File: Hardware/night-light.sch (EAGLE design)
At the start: 52 parts, among them Q1 8/16/20MHz, U1 ATMEGA328, U2 MIC5205

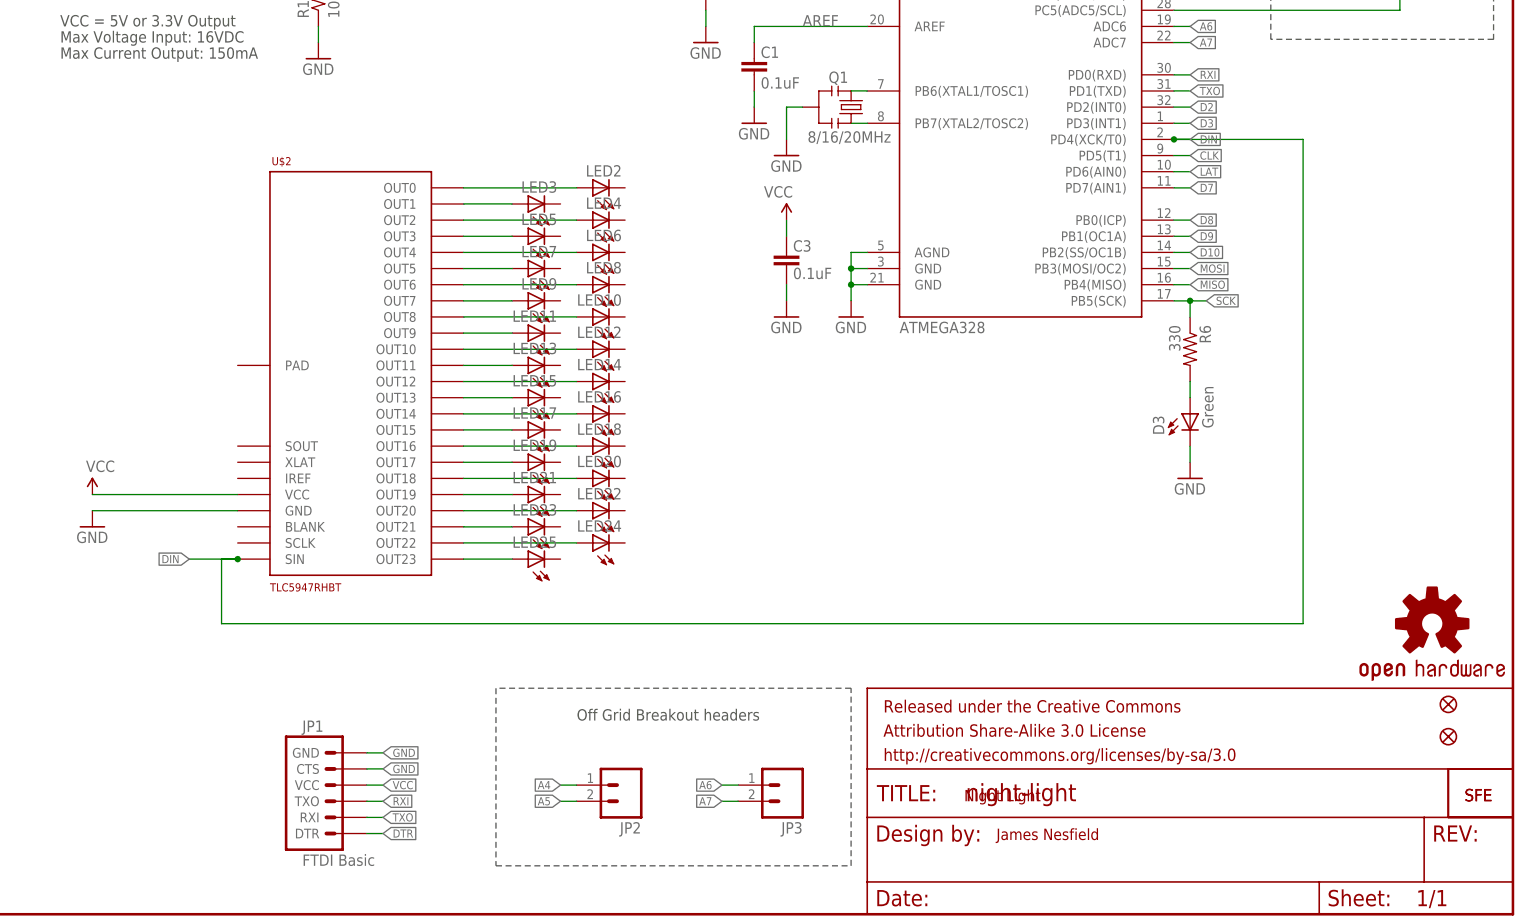
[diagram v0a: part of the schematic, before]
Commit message: added tlc5947
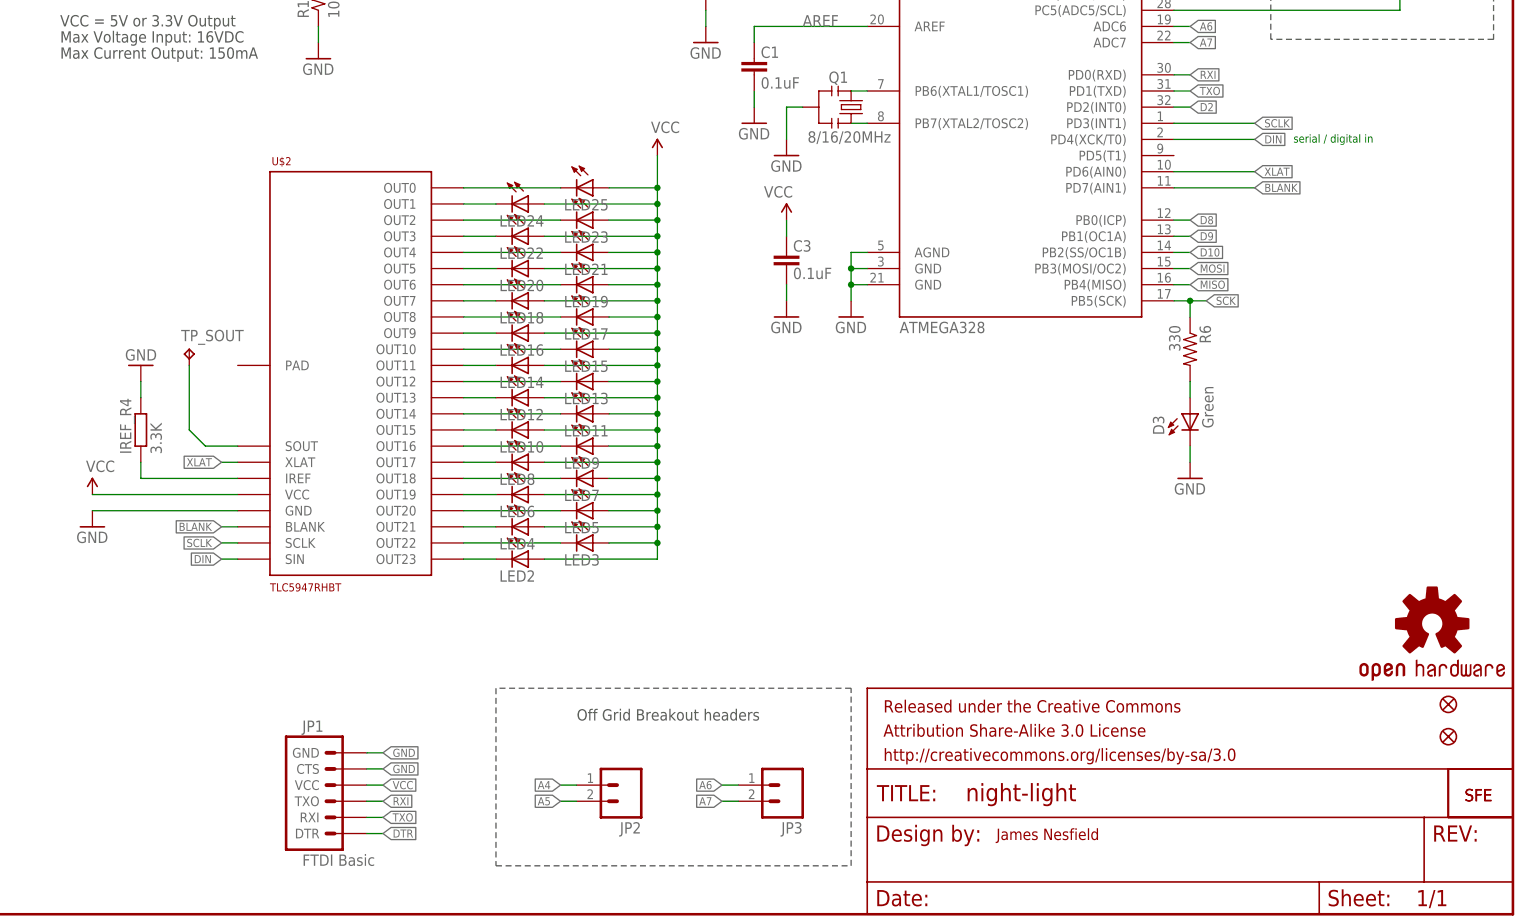
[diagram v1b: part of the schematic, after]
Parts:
- added IREF_R4: 3.3K, eagle-ltspice:RR0603
- added TP_SOUT: TPTP20R, testpad:TPTP20R
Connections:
- removed net CLK: U1.PD5(T1)
- removed net D3: U1.PD3(INT1)
- removed net D7: U1.PD7(AIN1)
- removed net LAT: U1.PD6(AIN0)
- new net BLANK: U$2.BLANK, U1.PD7(AIN1)
- new net N$30: LED3.C, U$2.OUT22
- new net N$31: LED2.C, U$2.OUT23
- new net SCLK: U$2.SCLK, U1.PD3(INT1)
- new net XLAT: U$2.XLAT, U1.PD6(AIN0)
- net 3.3V: now also LED10.A, LED11.A, LED12.A, LED13.A, LED14.A, LED15.A, LED16.A, LED17.A, LED18.A, LED19.A, LED2.A, LED20.A, LED21.A, LED22.A, LED23.A, LED24.A, LED25.A, LED3.A, LED4.A, LED5.A, LED6.A, LED7.A, LED8.A, LED9.A
- net GND: now also IREF_R4.2
- net N$10: now also LED23.C, U$2.OUT2; no longer LED6.A, U$2.OUT4
- net N$11: now also LED22.C, U$2.OUT3; no longer LED7.A, U$2.OUT5
- net N$12: now also LED21.C, U$2.OUT4; no longer LED8.A, U$2.OUT6
- net N$13: now also LED20.C, U$2.OUT5; no longer LED9.A, U$2.OUT7
- net N$14: now also LED19.C, U$2.OUT6; no longer LED10.A, U$2.OUT8
- net N$15: now also LED18.C, U$2.OUT7; no longer LED11.A, U$2.OUT9
- net N$16: now also LED17.C, U$2.OUT8; no longer LED12.A, U$2.OUT10
- net N$17: now also LED16.C, U$2.OUT9; no longer LED13.A, U$2.OUT11
- net N$18: now also LED15.C, U$2.OUT10; no longer LED14.A, U$2.OUT12
- net N$19: now also LED14.C, U$2.OUT11; no longer LED15.A, U$2.OUT13
- net N$20: now also LED13.C, U$2.OUT12; no longer LED16.A, U$2.OUT14
- net N$21: now also LED12.C, U$2.OUT13; no longer LED17.A, U$2.OUT15
- net N$22: now also LED11.C, U$2.OUT14; no longer LED18.A, U$2.OUT16
- net N$23: now also LED10.C, U$2.OUT15; no longer LED19.A, U$2.OUT17
- net N$24: now also LED9.C, U$2.OUT16; no longer LED20.A, U$2.OUT18
- net N$25: now also LED8.C, U$2.OUT17; no longer LED21.A, U$2.OUT19
- net N$26: now also LED7.C, U$2.OUT18; no longer LED22.A, U$2.OUT20
- net N$27: now also LED6.C, U$2.OUT19; no longer LED23.A, U$2.OUT21
- net N$28: now also LED5.C, U$2.OUT20; no longer LED24.A, U$2.OUT22
- net N$29: now also LED4.C, U$2.OUT21; no longer LED25.A, U$2.OUT23
- net N$5: now also LED25.C; no longer LED2.A
- net N$6: now also IREF_R4.1, U$2.IREF; no longer LED3.A, U$2.OUT1
- net N$8: now also LED24.C, U$2.OUT1; no longer LED4.A, U$2.OUT2
- net N$9: now also TP_SOUT.TP, U$2.SOUT; no longer LED5.A, U$2.OUT3
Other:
- note added: "serial / digital in"
- note removed: "Night Light"
- moved on the sheet: LED10, LED11, LED12, LED13, LED14, LED15, LED16, LED17, LED18, LED19, LED2, LED20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

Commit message: new pcb
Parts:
- removed C19: 10uF, SparkFun:CAP_POL1206
- removed C3: 0.1uF, SparkFun:CAP0603-CAP
- removed FRAME1: FRAME-LETTER, SparkFun-Aesthetics:FRAME-LETTER
- removed JP2, JP3: (no value), SparkFun:M02PTH
- removed LED1: Red, Testing:LED
- removed R1, R3: (no value), SparkFun:RESISTOR0603-RES
- removed R11: 10K, SparkFun:RESISTOR0603-RES
- removed SJ1: SOLDERJUMPERNC, SparkFun-Passives:SOLDERJUMPERNC
- removed U$1: LOGO-SFESK, SparkFun:LOGO-SFESK
- removed U$11: LOGO-SFENEW, SparkFun:LOGO-SFENEW
- removed U$3: OSHW-LOGOS, SparkFun:OSHW-LOGOS
- removed U2: MIC5205, SparkFun:V_REG_LDOSMD
- added C6, C7: 4.7uF, SparkFun-Capacitors:4.7UF-6.3V-10%(0603)0603
- added D1: RED, SparkFun-LED:LED-RED0603
- added JP4: M02PTH, SparkFun-Connectors:M02PTH
- added JP6: Micro USB, SparkFun-Connectors:USB-ABCONN-11794
- added JP7: JST, SparkFun-Connectors:JST_2MM_MALE
- added R5: 330, SparkFun-Resistors:330OHM1/10W1%(0603)
- added R7: 2.0k, SparkFun-Resistors:2.0KOHM1/10W5%(0603)
- added R8: (no value), SparkFun-Resistors:RESISTORPTH-1/4W-VERT-KIT
- added U4: MCP73831, SparkFun-PowerIC:MCP73831
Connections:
- net AREF renamed N$32
- removed net A4: JP2.1, R1.1, U1.PC4(ADC4/SDA)
- removed net A5: JP2.2, R3.1, U1.PC5(ADC5/SCL)
- removed net N$3: LED1.A, SJ1.1, U2.OUT
- removed net N$4: LED1.C, R11.2
- removed net RAW: C19.+, U2.EN, U2.IN
- new net 5V: C6.1, JP6.VBUS, R5.2, U4.VIN
- new net N$34: D1.A, R5.1
- new net PROG1: R7.1, R8.2, U4.PROG
- new net STAT1: D1.C, U4.STAT
- net A6: no longer JP3.1
- net A7: no longer JP3.2
- net GND: now also C6.2, C7.2, JP4.1, JP6.GND, JP7.-, R7.2, R8.1, U4.VSS; no longer C19.-, C3.1, R11.1, U2.GND
- net VCC: now also C7.1, JP4.2, JP7.+, U4.VBAT; no longer C3.2, R1.2, R3.2, SJ1.2
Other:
- note added: "0.1""
- note added: "Connection to 3.7V System"
- note added: "Lipo Battery"
- note added: "Set for 500mA charging"
- note added: "microUSB"
- note removed: "Max Current Output: 150mA"
- note removed: "Max Voltage Input: 16VDC"
- note removed: "Off Grid Breakout headers"
- note removed: "Optional Pullups for I2C lines"
- note removed: "VCC = 5V or 3.3V Output"
- moved on the sheet: C1, C10, C13, C2, D3, IREF_R4, JP1, LED10, LED11, LED12, LED13, LED14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
